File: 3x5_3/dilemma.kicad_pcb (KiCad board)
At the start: 2 copper layers, 134.1 x 215.7 mm, 89 parts, among them J5001 BATTERY_CONN_DEANS, J5011 BATTERY_CONN_DEANS, SW101 NA_SW_Push, SW102 NA_SW_Push, SW103 NA_SW_Push, SW104 NA_SW_Push, SW105 NA_SW_Push, SW106 NA_SW_Push, SW107 NA_SW_Push, SW108 NA_SW_Push, SW109 NA_SW_Push, SW112 NA_SW_Push, SW113 NA_SW_Push, SW114 NA_SW_Push, SW115 NA_SW_Push, SW116 NA_SW_Push, SW117 NA_SW_Push, SW118 NA_SW_Push, SW119 NA_SW_Push, SW3001 NA_SW_Push, SW5002 NA_SW_Push, SW5003 NA_SW_Push, SW5004 NA_SW_Push, SW5005 NA_SW_Push, SW5006 NA_SW_Push, SW5007 NA_SW_Push, SW5008 NA_SW_Push, SW5009 NA_SW_Push, SW5010 NA_SW_Push, SW5011 NA_SW_Push, SW5012 NA_SW_Push, SW5013 NA_SW_Push, SW5014 NA_SW_Push, SW5015 NA_SW_Push, SW5016 NA_SW_Push, SW5017 NA_SW_Push, SW5018 NA_SW_Push, SW5019 NA_SW_Push, SW5021 SW_SPST, SW5022 SW_SPST, U5001 eliteC, U5007 eliteC

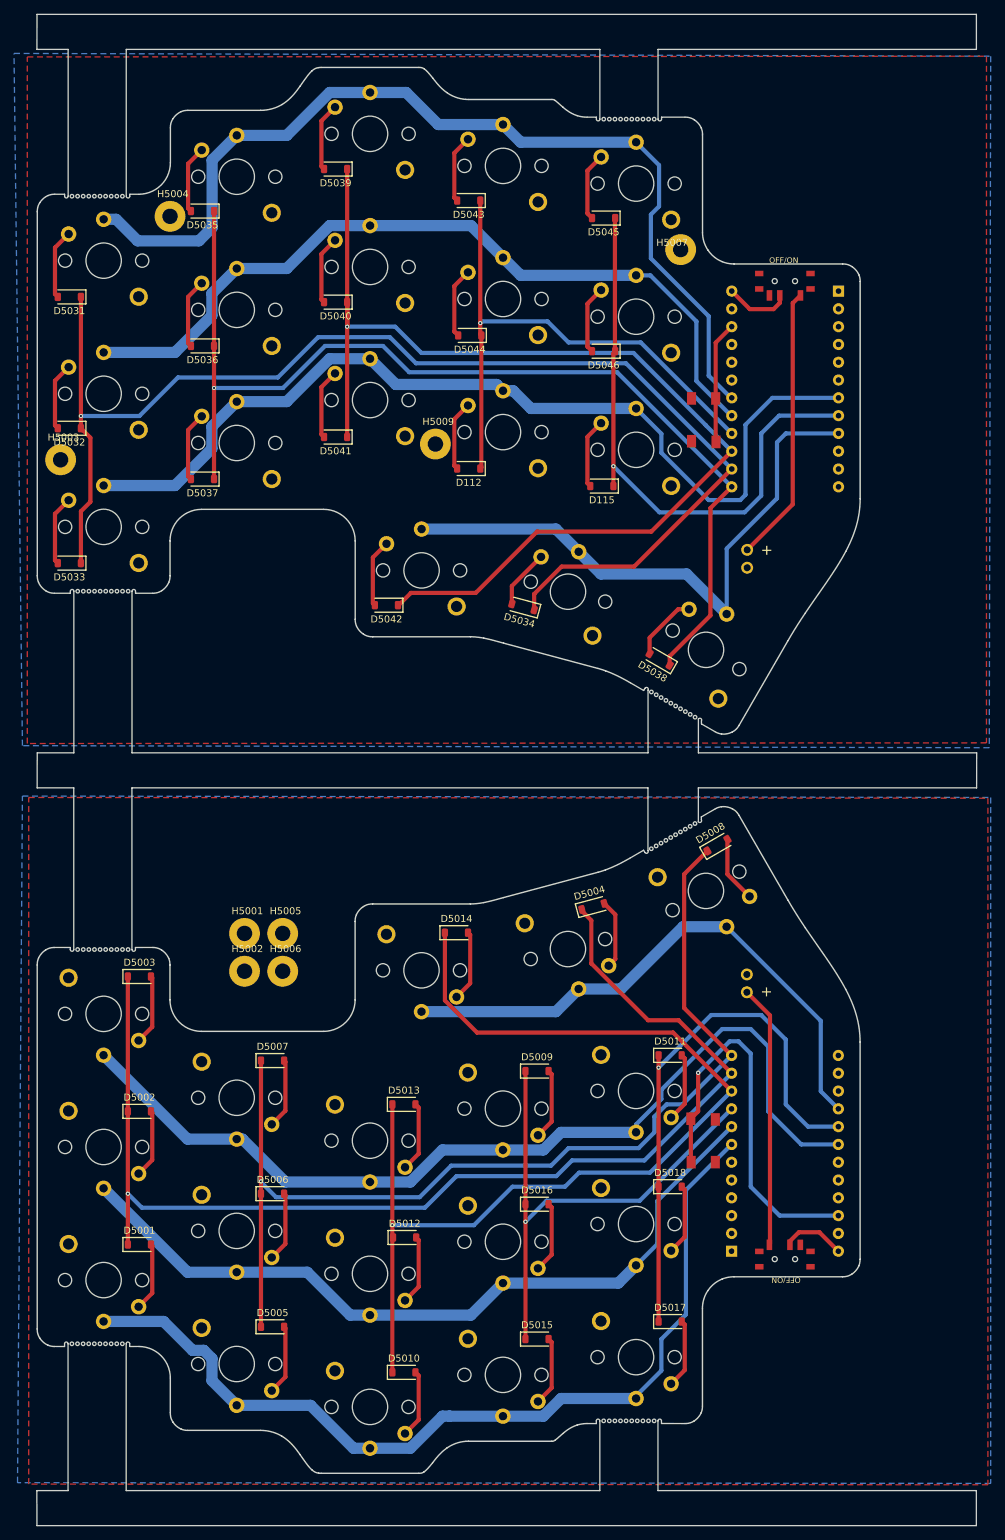
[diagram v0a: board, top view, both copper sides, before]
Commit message: adjust edge cuts
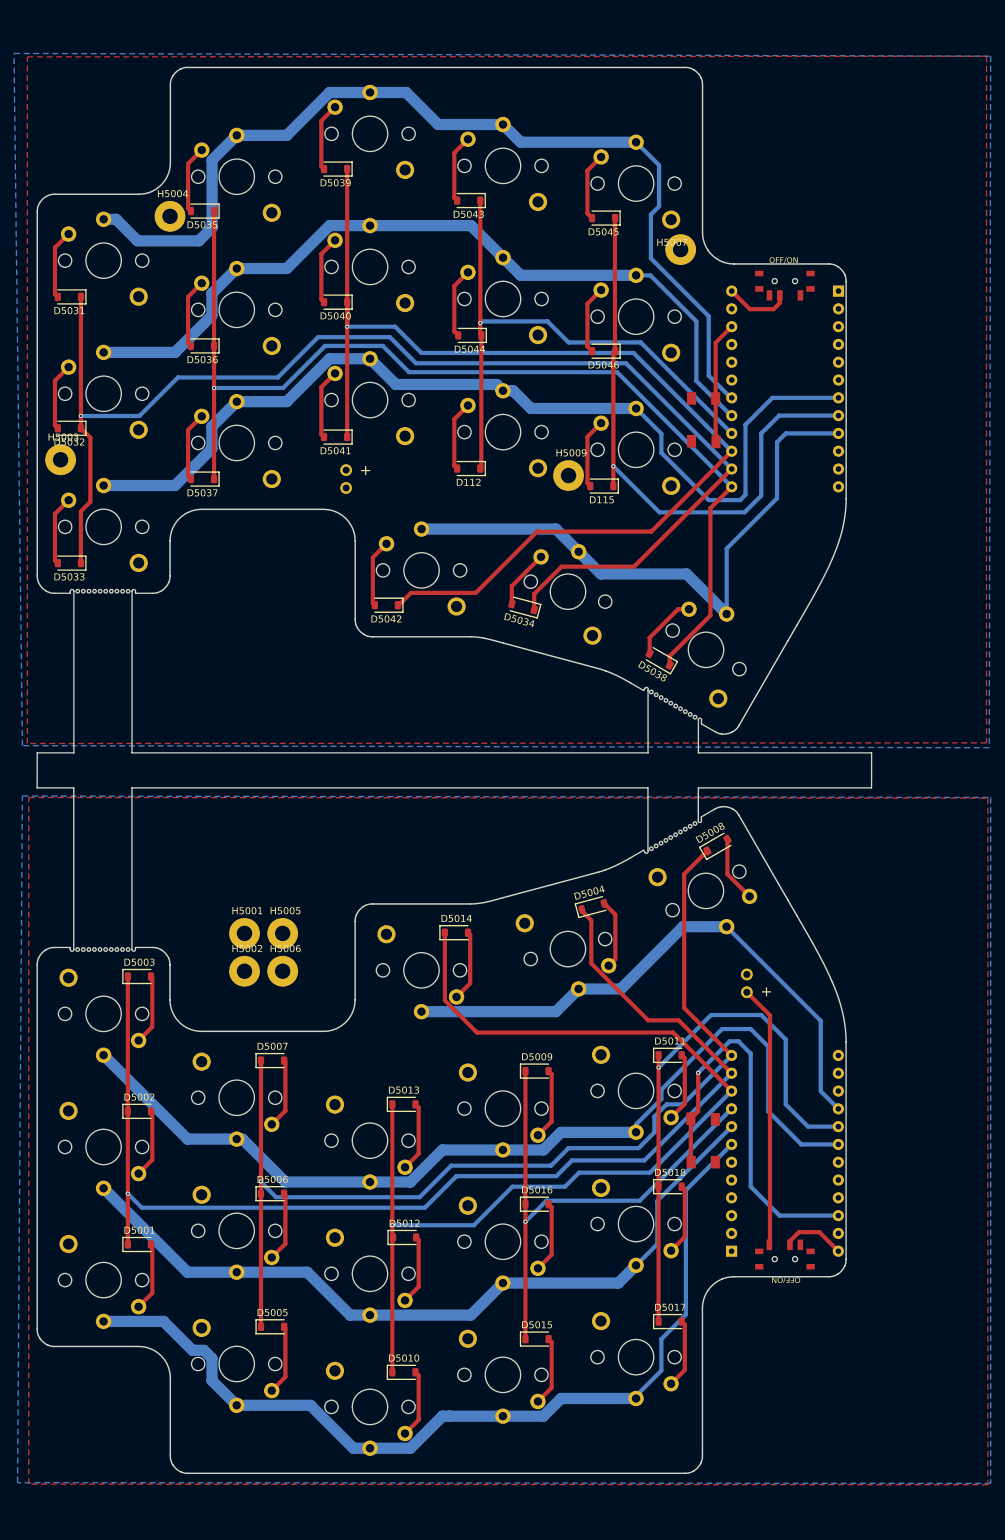
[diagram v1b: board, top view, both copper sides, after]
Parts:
- moved J5011 58.4 mm to (156.5, 86.2)
- moved H5009 19.5 mm to (188.2, 84.4)
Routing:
- net BAT_SW: track 39.5 -> 0.00 mm
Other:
- board size 134.1 x 215.7 mm -> 119.1 x 200.7 mm

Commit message: reroute
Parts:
- moved J5001 71.8 mm to (190.0, 223.4), turned to 90 degrees
- moved J5011 64.6 mm to (187.2, 29.4), turned to 90 degrees
- moved PSW5002 35.0 mm to (199.0, 225.0)
- moved PSW5001 35.0 mm to (199.0, 28.0)
- moved SW5021 23.7 mm to (217.7, 157.9), turned to 180 degrees
- moved SW5022 21.6 mm to (218.0, 95.4), turned to 0 degrees
- moved U5007 1.29 mm to (210.2, 86.0)
- moved U5001 1.26 mm to (225.5, 167.2)
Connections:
- PSW5001 pad 1: BAT_SW -> BAT
- PSW5001 pad 2: BAT -> BAT_SW
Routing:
- net RESET_L: track 56.5 -> 0.00 mm, vias 1 -> 0
- net BAT_L: track 9.09 -> 48.3 mm
- net BAT: track 9.38 -> 35.8 mm
- net BAT_SW_L: track 37.5 -> 11.4 mm
- net RESET: track 17.4 -> 0.00 mm
- net BAT_SW: track 0.00 -> 11.2 mm
- net M_COL3: track 164.3 -> 156.5 mm
- net M_ROW4_L: track 135.1 -> 132.0 mm
- net M_COL5_L: track 78.8 -> 75.8 mm
- net M_ROW1: track 85.4 -> 84.1 mm
- net M_COL5: track 84.1 -> 82.9 mm
- net M_ROW4: track 136.1 -> 135.1 mm
- net M_COL4_L: track 74.3 -> 73.4 mm
- net M_COL4: track 81.0 -> 80.3 mm
- net M_COL2_L: track 149.2 -> 148.6 mm
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
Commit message: finish layout
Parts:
- moved H5005 76.3 mm to (204.2, 200.7)
- moved H5002 51.4 mm to (131.2, 205.4)
- moved H5006 43.2 mm to (188.5, 168.7)
- moved H5001 33.6 mm to (115.7, 170.7)
- moved SW5021 0.25 mm to (218.0, 157.9)
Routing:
- net RESET: track 0.00 -> 38.6 mm
- net RESET_L: track 0.00 -> 38.4 mm
- net M_ROW2_L: track 129.7 -> 141.2 mm
- net BAT_L: track 48.3 -> 52.0 mm
- net M_COL5_L: track 75.8 -> 77.3 mm
- net M_COL2_L: track 148.6 -> 149.8 mm
- net M_COL1_L: track 167.9 -> 169.1 mm
- net M_COL5: track 82.9 -> 84.0 mm
- net M_COL4: track 80.3 -> 81.2 mm
- net M_COL4_L: track 73.4 -> 74.1 mm

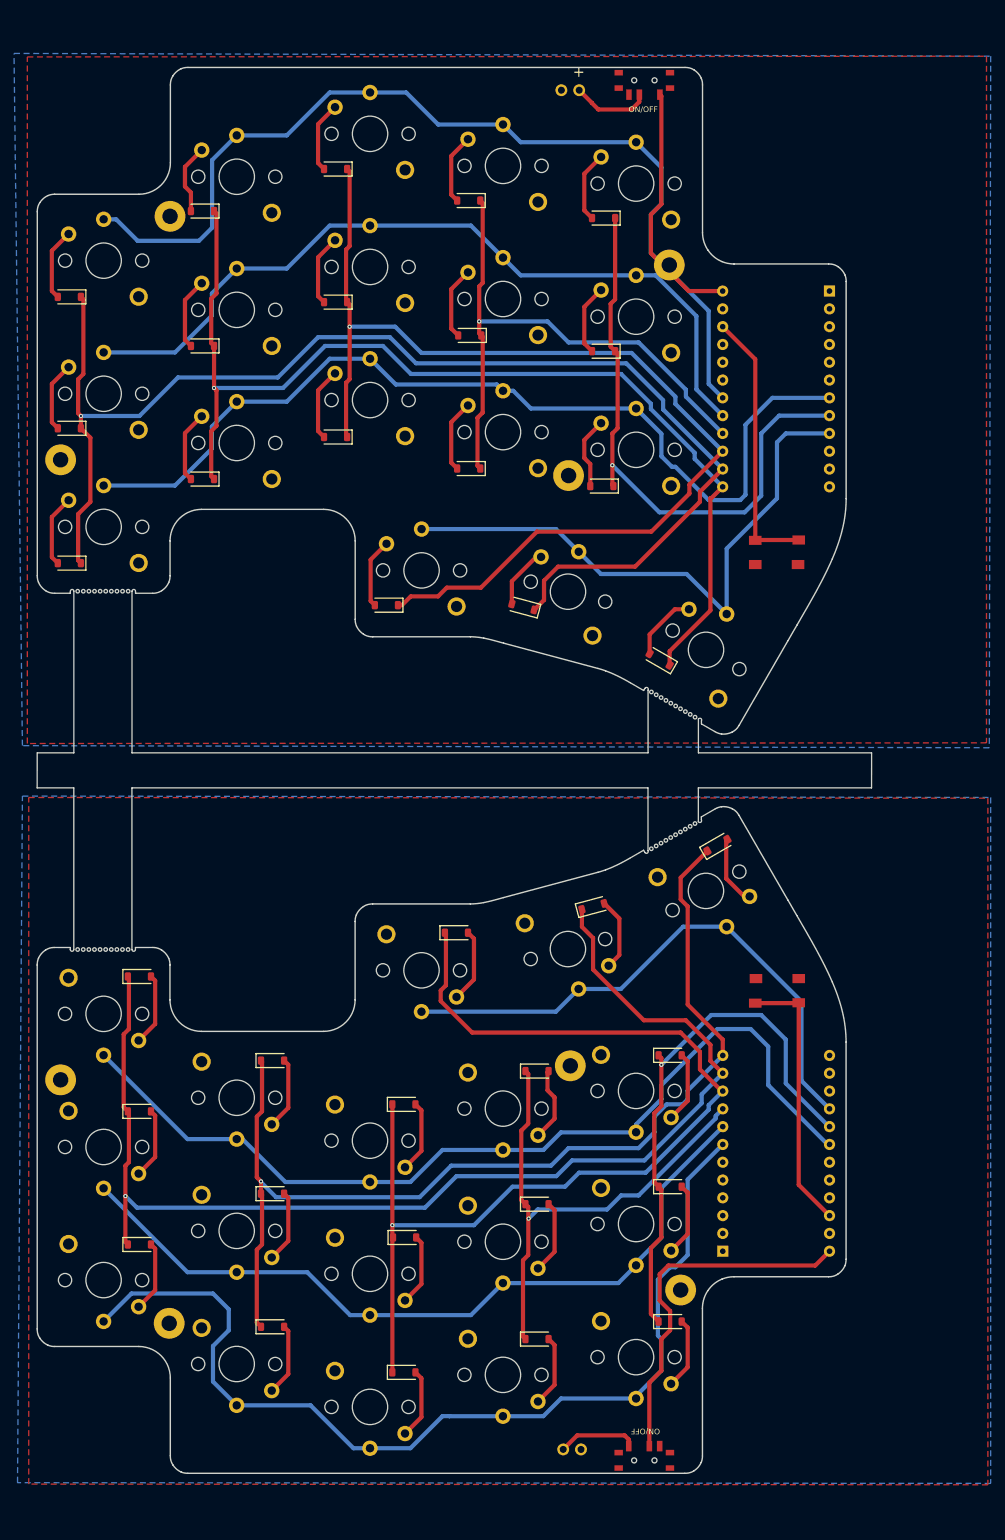
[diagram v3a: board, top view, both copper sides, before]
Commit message: case clearance & plate
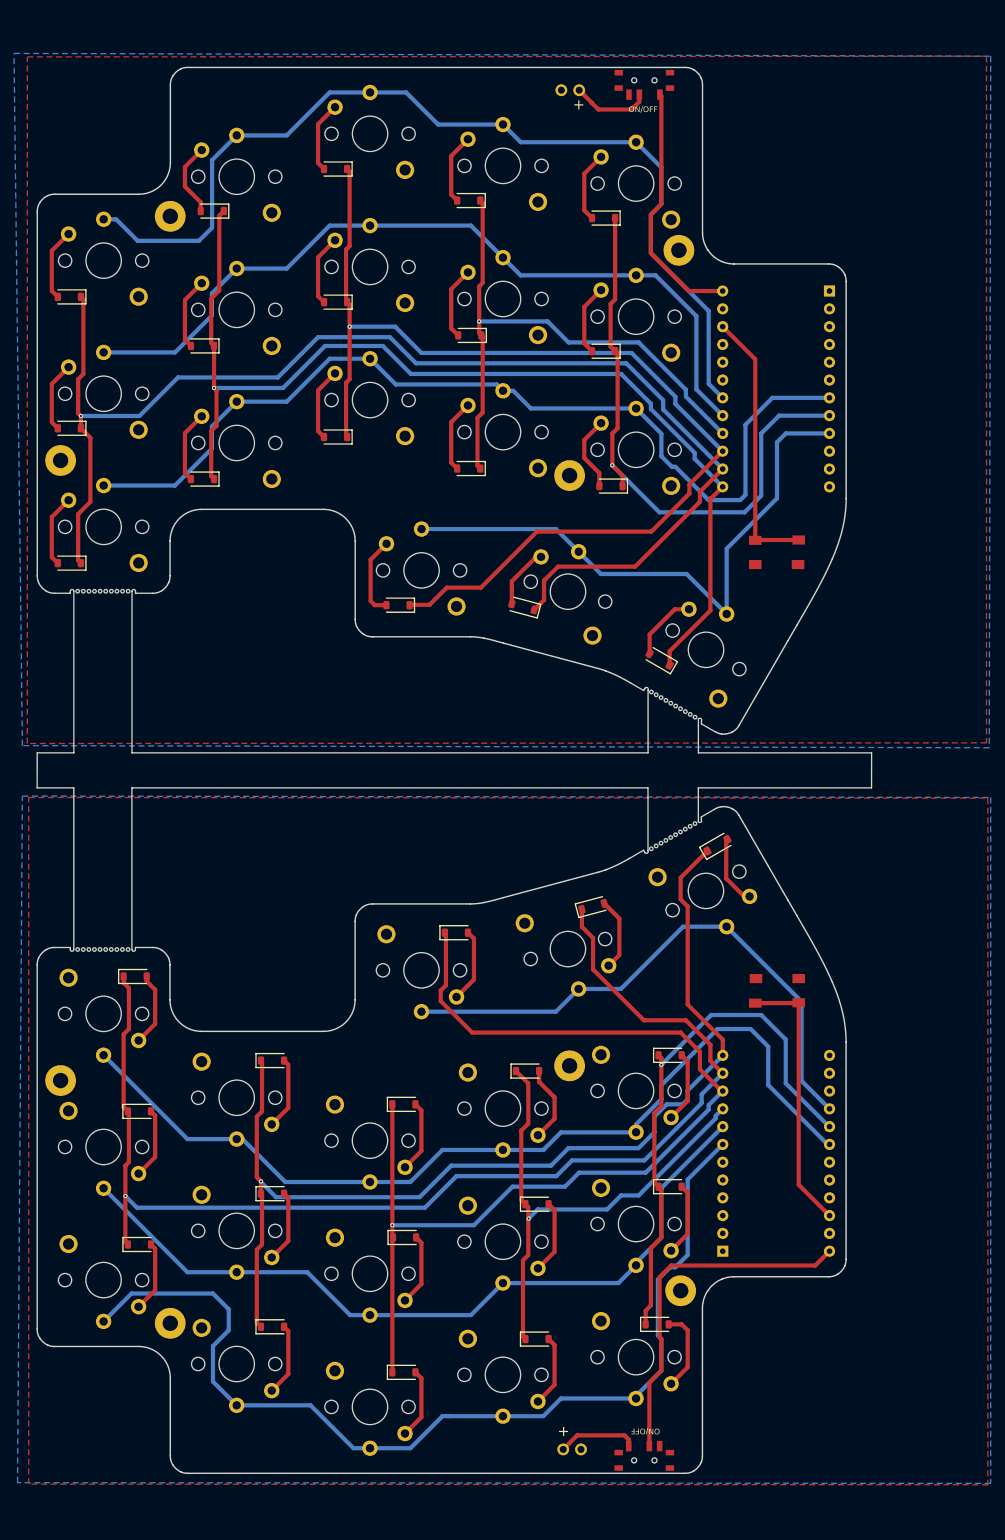
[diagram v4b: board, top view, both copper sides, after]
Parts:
- removed BT5001: Battery, 0xB2_drawings:LP602945-PCM-LD-A14348
- moved H5007 2.51 mm to (204.0, 52.3)
- moved D5017 1.89 mm to (200.9, 205.6)
- moved D5042 1.65 mm to (163.9, 102.9)
- moved D5035 1.40 mm to (137.4, 46.7)
- moved D5009 1.35 mm to (182.4, 169.4)
- moved D115 1.30 mm to (194.3, 85.9)
- moved D5003 0.60 mm to (126.4, 155.9)
- moved H5002 0.15 mm to (131.4, 205.4)
- moved H5009 0.15 mm to (188.4, 84.4)
- moved H5001 0.10 mm to (115.7, 170.8)
- moved H5003 0.10 mm to (115.7, 82.3)
- moved H5005 0.10 mm to (204.2, 200.8)
- moved H5006 0.10 mm to (188.4, 168.7)
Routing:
- net Net-(D5042-A): track 9.95 -> 11.6 mm
- net M_COL3: track 156.5 -> 154.9 mm
- net Net-(D5017-A): track 10.2 -> 11.7 mm
- net BAT_L: track 52.0 -> 50.7 mm
- net Net-(D5035-A): track 10.0 -> 10.6 mm
- net M_COL4_L: track 74.1 -> 74.7 mm
- net Net-(D115-A): track 10.3 -> 10.9 mm
- net M_COL5: track 84.0 -> 84.5 mm

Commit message: adjust nicenano .gitignore & fix on/off silkscreen
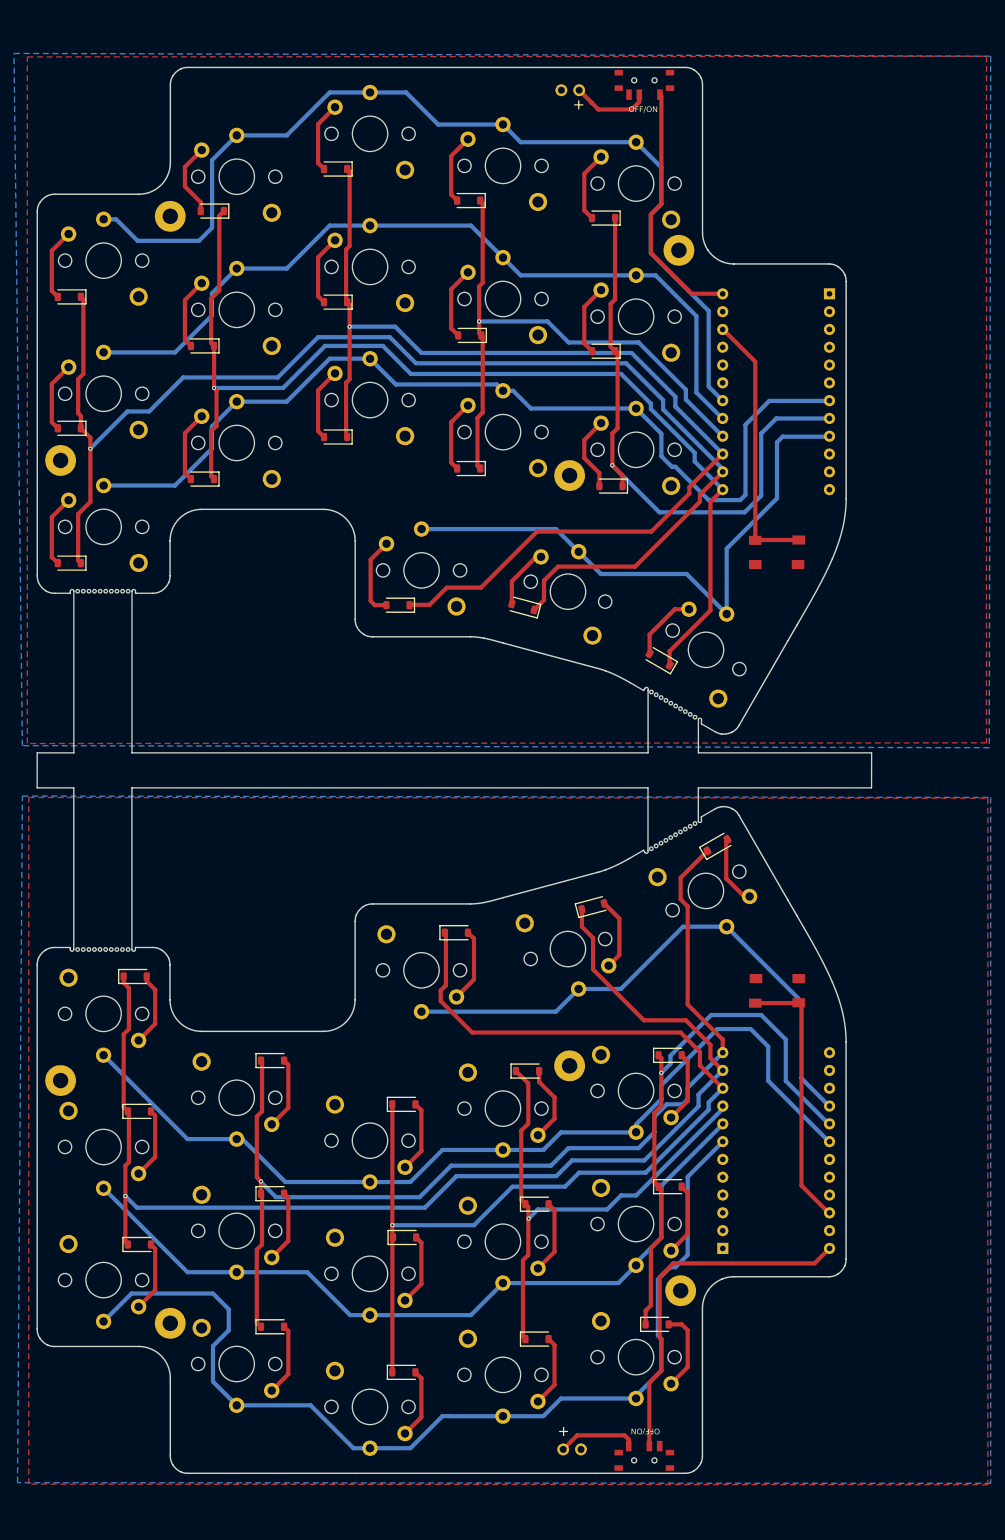
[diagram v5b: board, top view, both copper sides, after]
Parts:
- moved U5001 0.40 mm to (225.5, 166.8)
- moved U5007 0.40 mm to (210.2, 86.4)
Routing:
- net M_COL5_L: track 77.5 -> 78.3 mm
- net M_COL1: track 182.6 -> 183.2 mm
